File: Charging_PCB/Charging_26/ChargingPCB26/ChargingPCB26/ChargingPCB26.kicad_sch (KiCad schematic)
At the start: 48 parts, among them J1 Molex6pin, J2 Molex6pin, K101 Relay_SPDT_Omron_G2RL-1, K102 Relay_SPDT_Omron_G2RL-1, Q1 NMOS, Q103 Q_NPN_BEC, Q104 Q_NPN_BEC, Q105 Q_NPN_BEC, Q106 Q_NPN_BEC, Q2 NMOS, SW101 SW_Omron_B3FS, SW102 SW_Omron_B3FS, U1 SFH617A-1, U107 LM7805_TO220, U2 SFH617A-1, U5 74LS279, U6 74HC00

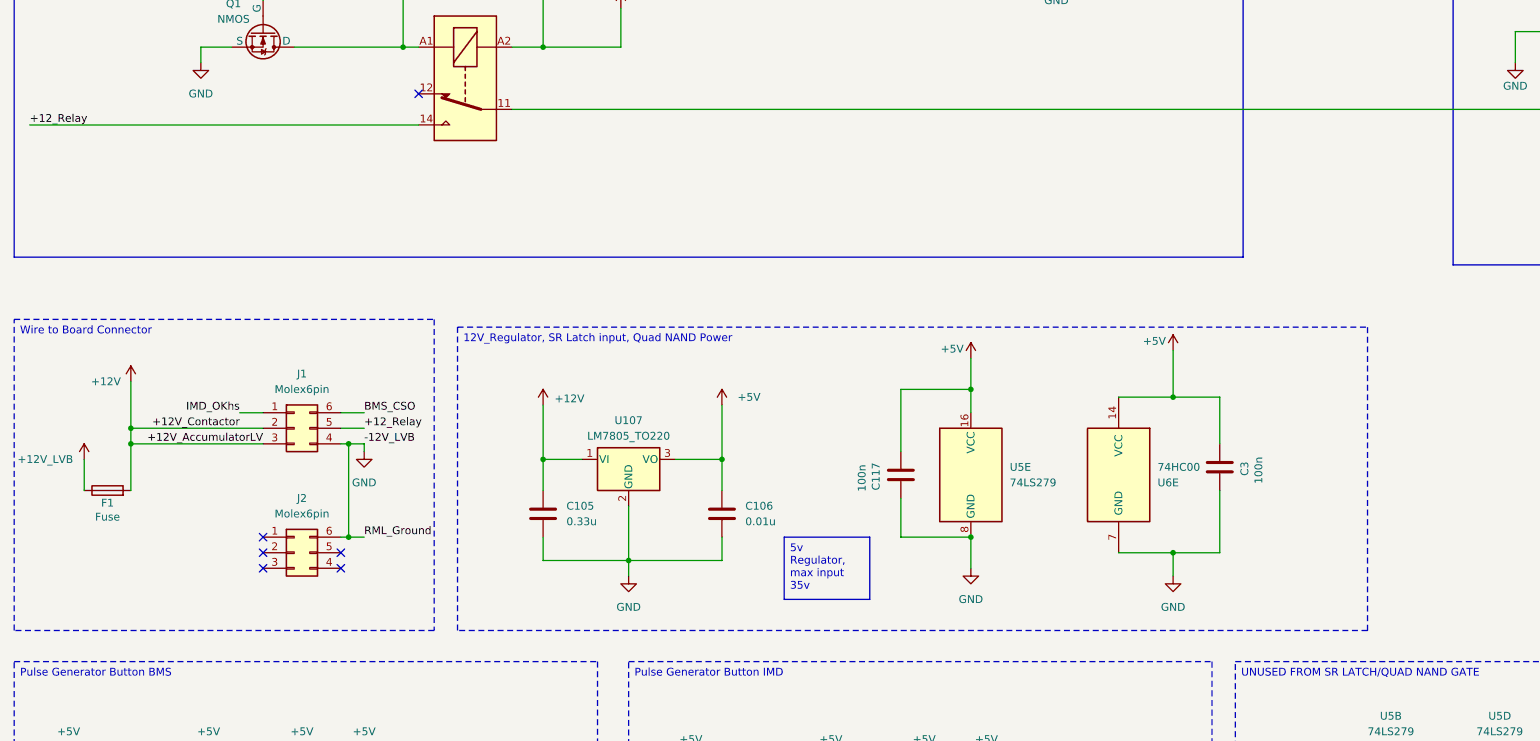
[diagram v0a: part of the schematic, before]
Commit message: fixed connector wiring
fuse is off board
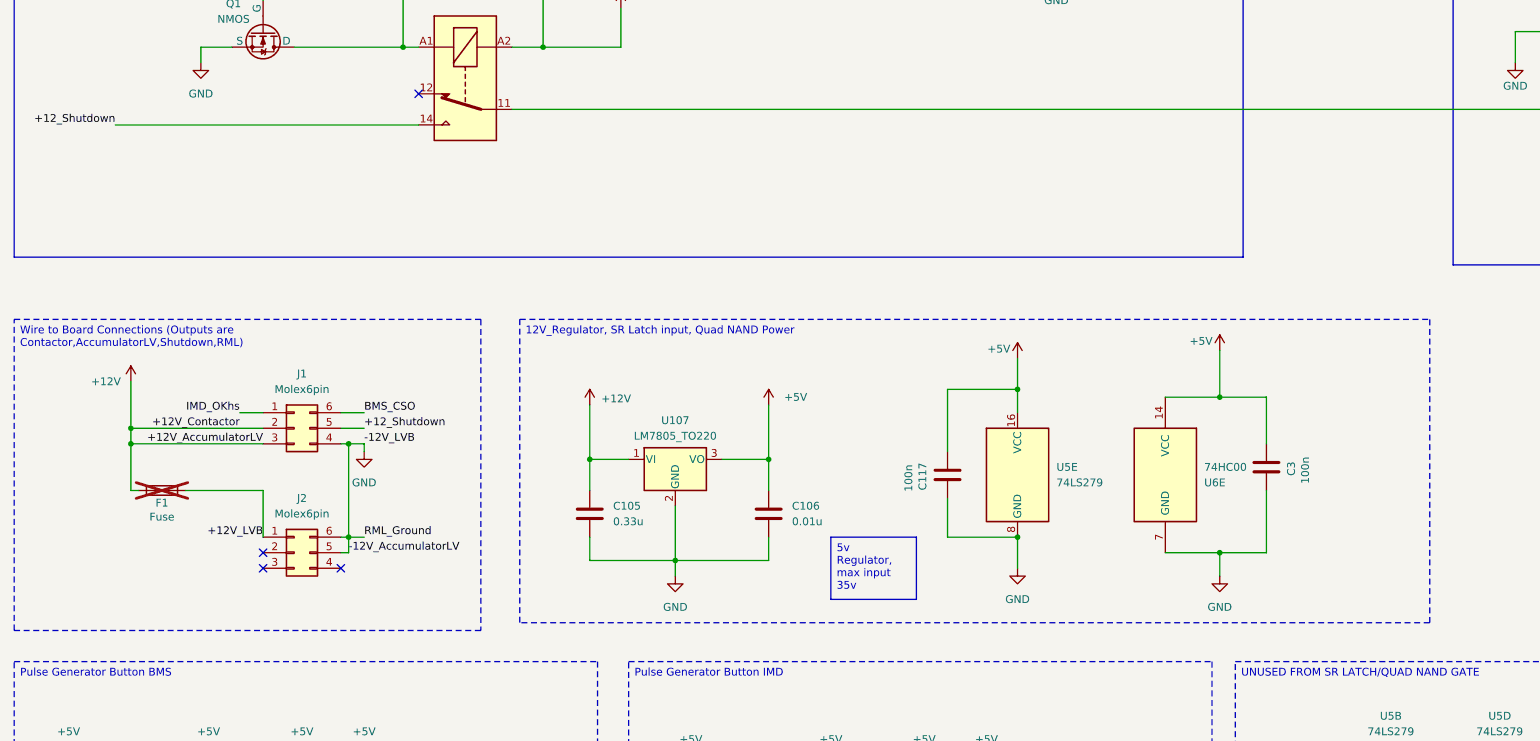
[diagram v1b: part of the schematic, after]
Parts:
- F1: now not fitted
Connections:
- net +12V: now also F1.1; no longer F1.2
- net +12V_LVB: now also F1.2, J2.1 (Pin_1); no longer F1.1
- net GND: now also J2.5 (Pin_5)
- net +12_Relay renamed +12_Shutdown
- no-connect marks 19 -> 17
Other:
- moved on the sheet: C105, C106, C117, C3, U107, U5E, U6E
